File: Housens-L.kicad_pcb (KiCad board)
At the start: 4 copper layers, 50 x 50 mm, 47 parts, among them J1 JTAG/SWD, J2 USB_C_2.0, Q1 BSS138DWQ, SW1 RESET, SW2 USER, U1 MCP1603, U2 BME280, U3 OPT3005, U4 STM32WB55CGUx, U5 STCC4, U6 REG710NA-3.3, Y1 32MHz, Y2 32.768kHz

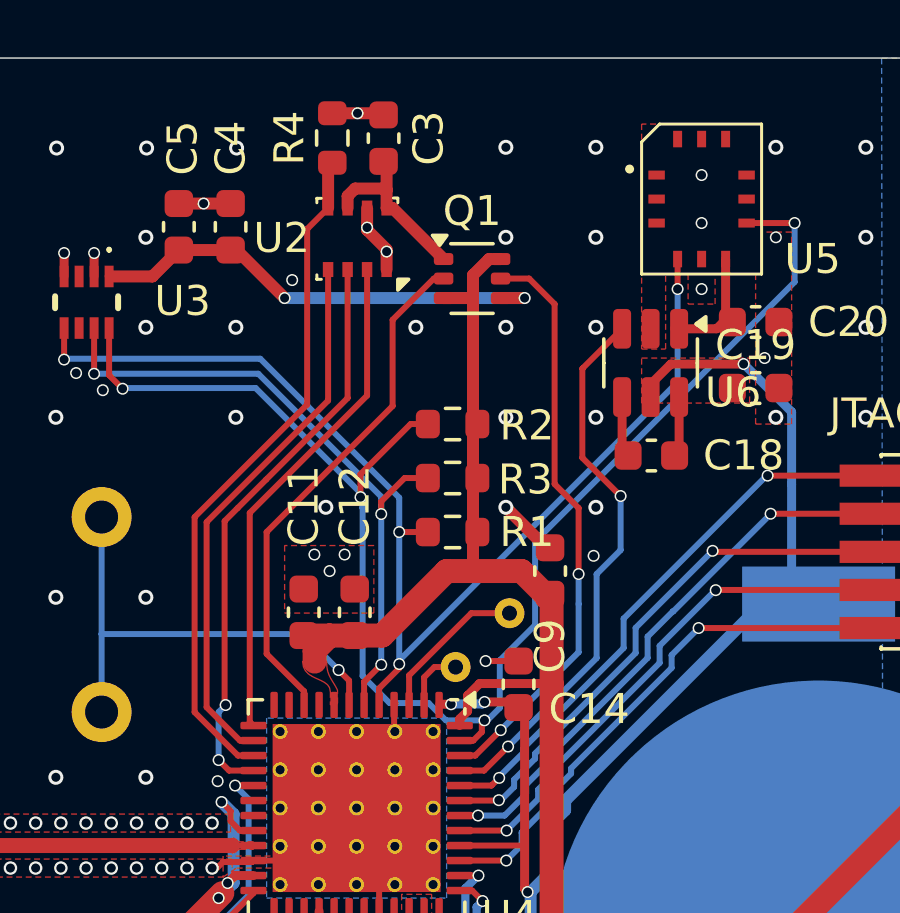
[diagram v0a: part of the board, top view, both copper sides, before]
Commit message: Use proper load switch instead of plain FET
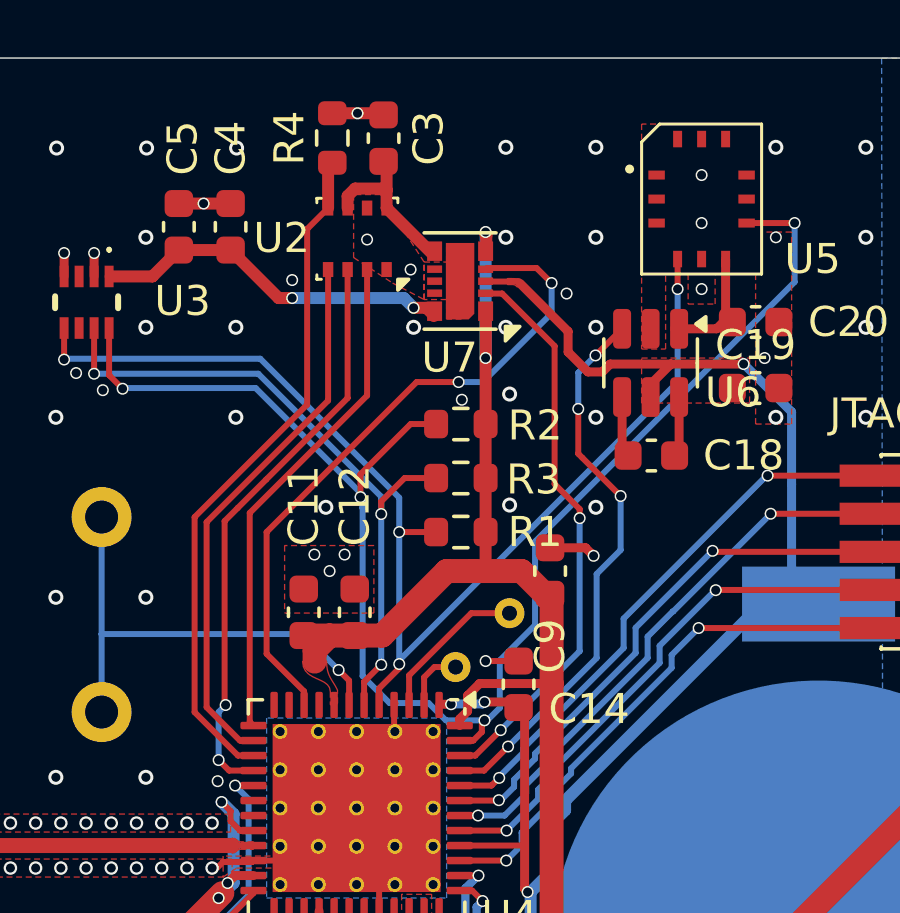
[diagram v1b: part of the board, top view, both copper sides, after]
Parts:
- removed Q1: BSS138DWQ, Package_TO_SOT_SMD:SOT-363_SC-70-6
- added U7: AP22966, Invented:DFN-14-1EP_3x2mm_P0.4mm_EP1.78x1.35mm_AP22966, F.Cu at (88.5, 87.4)
- moved R1 0.27 mm to (88.5, 95.8)
- moved R2 0.27 mm to (88.5, 92.2)
- moved R3 0.27 mm to (88.5, 94.0)
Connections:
- AE1 pad 2: GND -> (no net)
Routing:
- net +BATT: track 55.4 -> 63.2 mm
- net /~{ATMO_EN}: track 17.4 -> 22.2 mm, vias 0 -> 2
- net Net-(U3-VDD): track 15.6 -> 12.1 mm
- net GND: track 44.4 -> 41.6 mm, vias 164 -> 166
- net +1V8: track 109.1 -> 109.7 mm, vias 3 -> 5
- net /~{CO2_EN}: track 18.5 -> 18.6 mm, vias 2 -> 4

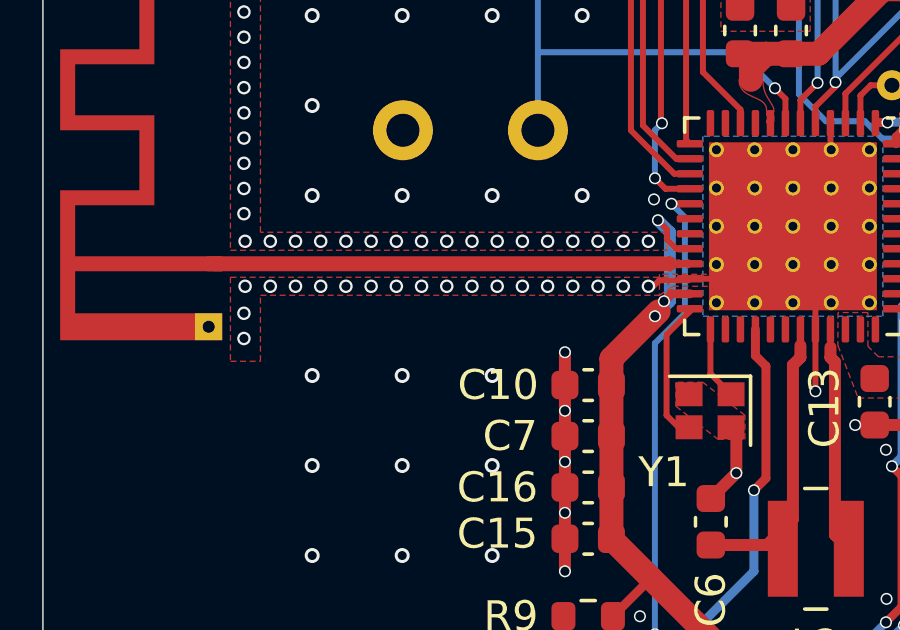
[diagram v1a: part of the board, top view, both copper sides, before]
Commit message: Add matching circuit to antenna
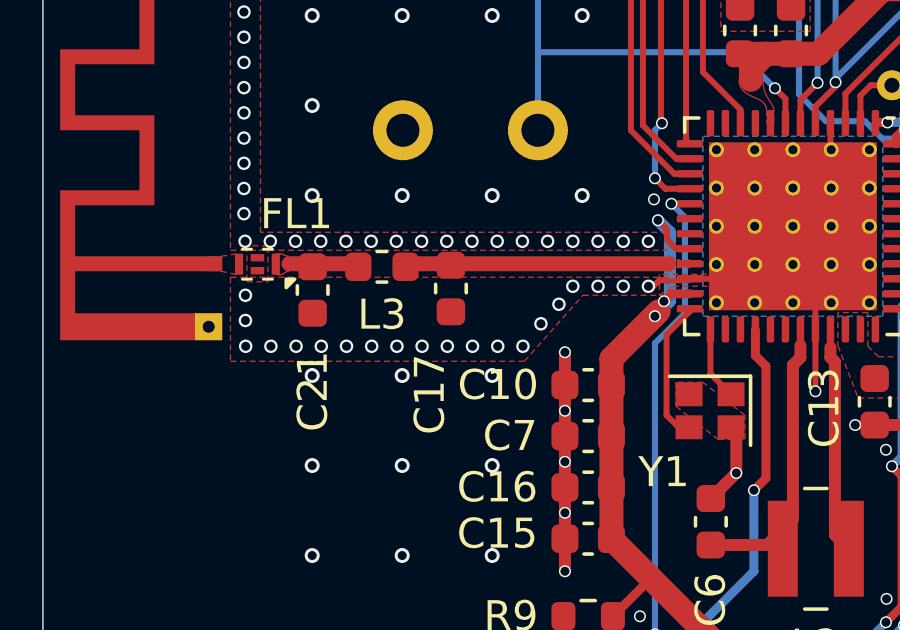
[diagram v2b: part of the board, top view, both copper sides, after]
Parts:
- added C17: 0.8p, Capacitor_SMD:C_0603_1608Metric, F.Cu at (73.6, 107.1)
- added C21: 0.3p, Capacitor_SMD:C_0603_1608Metric, F.Cu at (69.0, 107.1)
- added FL1: DLF162500LT-5028A1, Invented:DLF162500LT-5028A1, F.Cu at (67.2, 106.3)
- added L3: 2.7n, Inductor_SMD:L_0603_1608Metric, F.Cu at (71.3, 106.3)
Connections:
- U4 pad 21: Net-(AE1-A) -> Net-(U4-RF1)
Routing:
- net Net-(AE1-A): track 15.8 -> 0.00 mm
- net Net-(U4-RF1): track 0.00 -> 8.66 mm
- net Net-(FL1-IN): track 0.00 -> 2.35 mm
- net GND: vias 166 -> 167
- added copper zone on F.Cu, net Net-(FL1-IN)
- added copper zone on F.Cu, net Net-(U4-RF1)

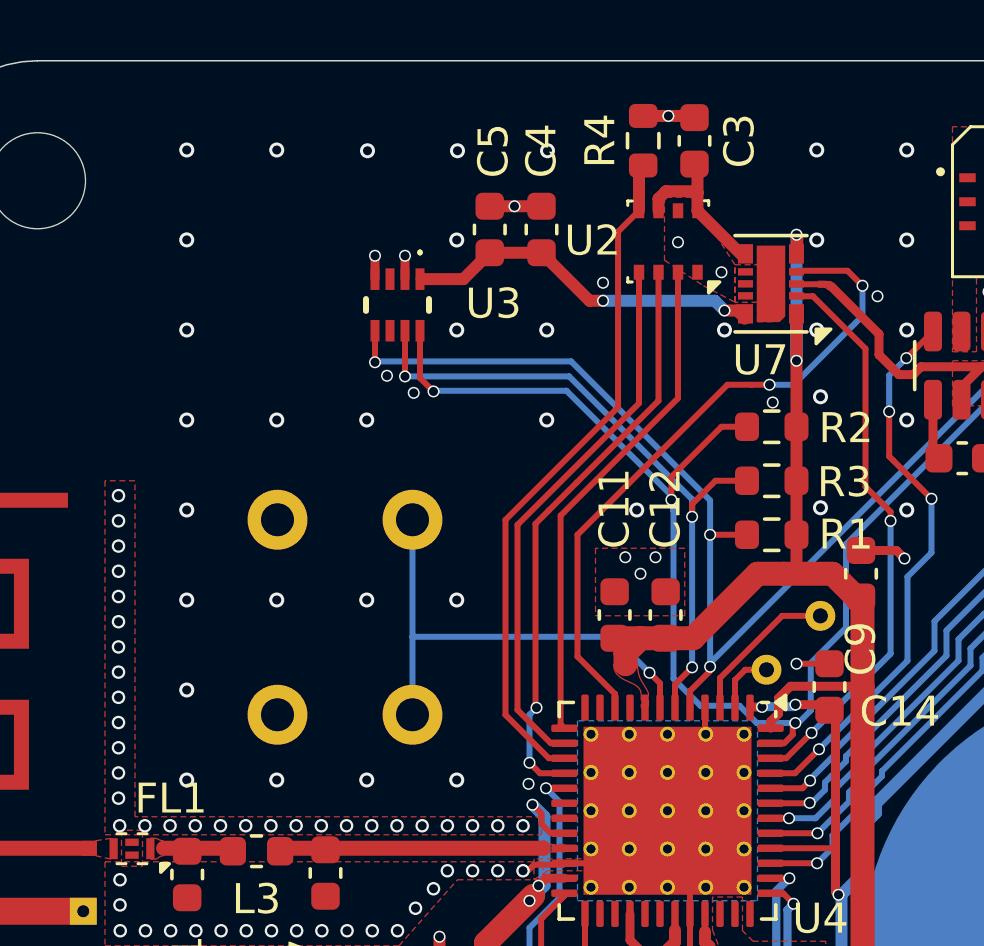
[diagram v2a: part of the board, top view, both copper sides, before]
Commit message: Space out the sensors
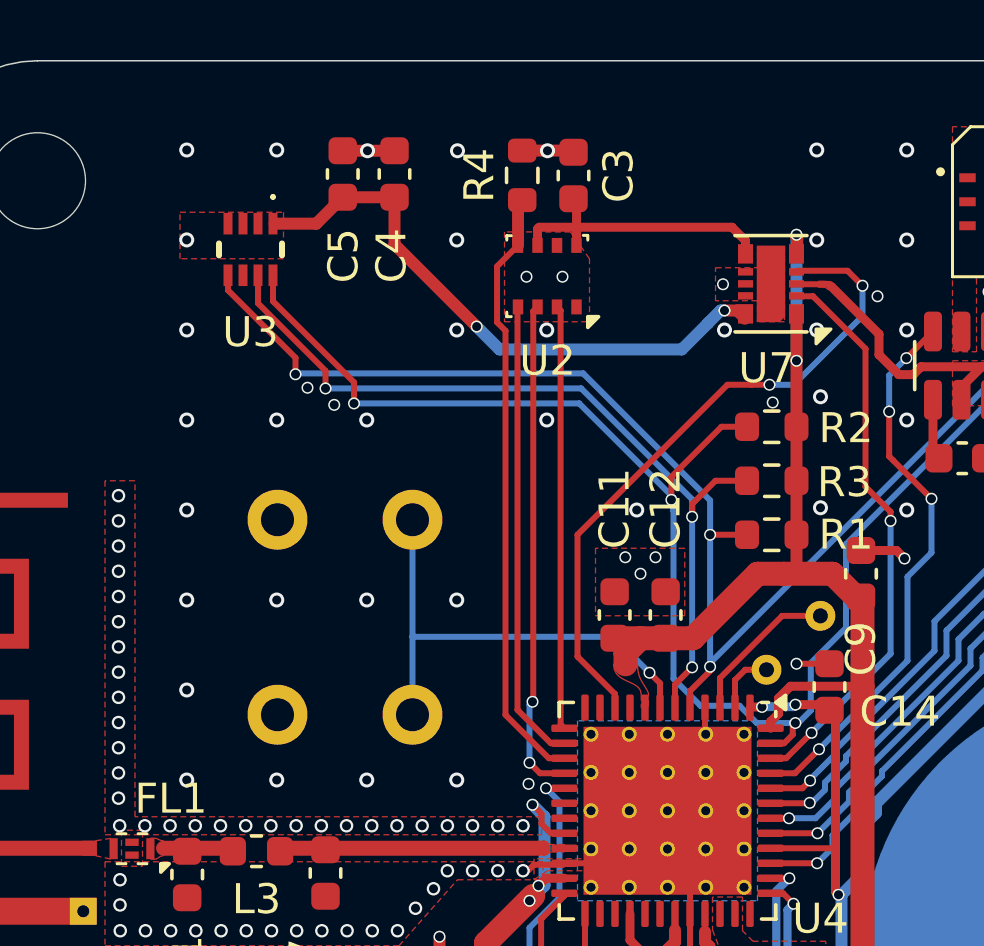
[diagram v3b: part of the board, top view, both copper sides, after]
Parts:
- moved C5 5.24 mm to (74.2, 83.8)
- moved U3 5.24 mm to (71.1, 86.3)
- moved C4 5.24 mm to (75.9, 83.8)
- moved C3 4.19 mm to (81.9, 83.8)
- moved R4 4.19 mm to (80.2, 83.8)
- moved U2 4.19 mm to (81.0, 87.2)
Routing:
- net Net-(U3-VDD): track 12.1 -> 19.7 mm
- net /I2C1_SCL: track 39.6 -> 45.3 mm
- net /OPT_INT: track 22.3 -> 27.9 mm
- net /I2C1_SDA: track 50.3 -> 55.9 mm
- net Net-(U2-VDD): track 5.56 -> 9.56 mm
- net /SPI1_SDO: track 19.5 -> 16.6 mm
- net /SPI1_CLK: track 18.3 -> 15.5 mm
- net /SPI1_CS: track 16.9 -> 14.1 mm
- net /SPI1_SDI: track 22.8 -> 20.2 mm
- net GND: track 41.6 -> 40.0 mm, vias 167 -> 163

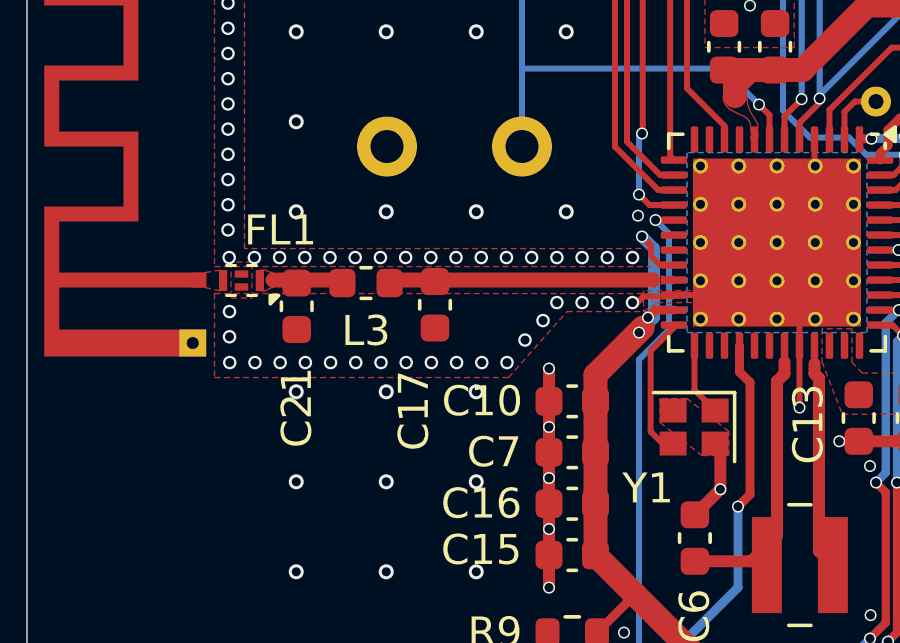
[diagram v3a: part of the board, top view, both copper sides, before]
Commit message: Replace matching circuit with IPD
This is more compact, purpose-made, and cheaper than the individual components!
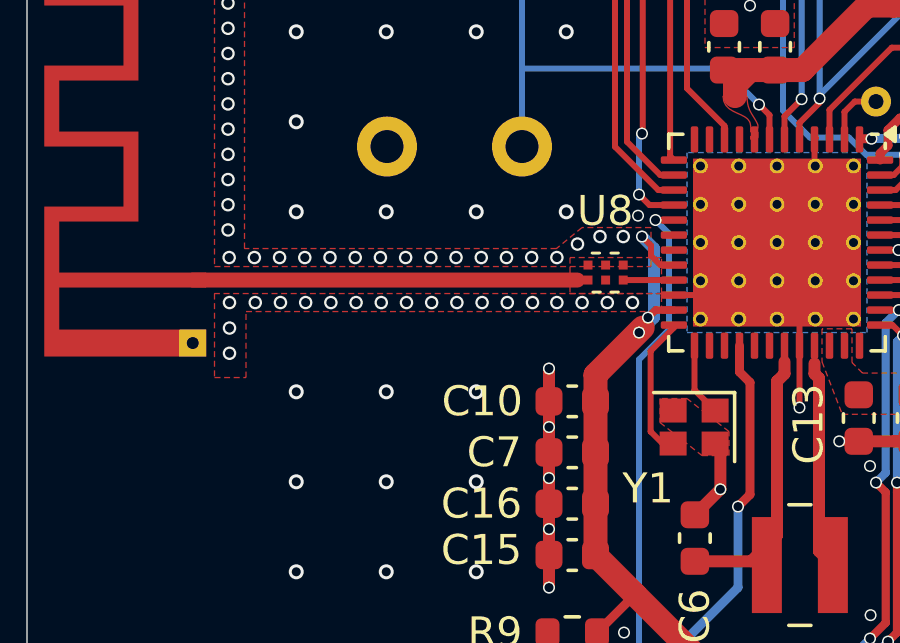
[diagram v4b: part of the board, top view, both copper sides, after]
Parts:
- removed C17: 0.8p, Capacitor_SMD:C_0603_1608Metric
- removed C21: 0.3p, Capacitor_SMD:C_0603_1608Metric
- removed FL1: DLF162500LT-5028A1, Invented:DLF162500LT-5028A1
- removed L3: 2.7n, Inductor_SMD:L_0603_1608Metric
- added U8: MLPF-WB55-01E3, Invented:MLPF-WB55-01E3, F.Cu at (79.3, 106.0)
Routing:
- net Net-(AE1-A): track 0.00 -> 12.3 mm
- net Net-(U4-RF1): track 8.66 -> 1.69 mm
- net Net-(FL1-IN): track 2.35 -> 0.00 mm
- net GND: track 40.0 -> 38.7 mm, vias 163 -> 162
- removed copper zone on F.Cu, net Net-(AE1-A)
- removed copper zone on F.Cu, net Net-(FL1-IN)
- removed copper zone on F.Cu, net Net-(U4-RF1)

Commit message: Use LM voltage reg instead of unobtainium MCP
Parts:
- U1: value MCP1603 -> LM3670MF; footprint Package_TO_SOT_SMD:SOT-23-5 -> Package_TO_SOT_SMD:TSOT-23-5

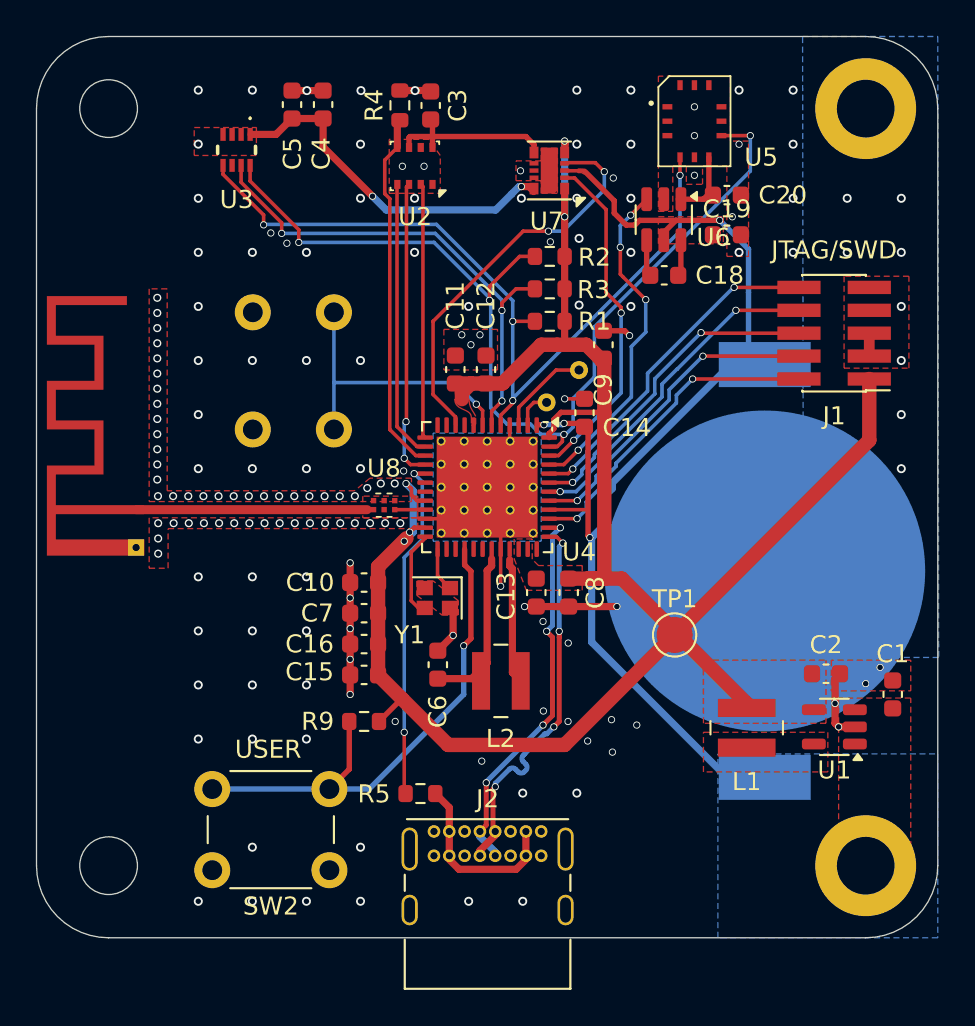
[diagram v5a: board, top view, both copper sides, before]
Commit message: Add RPi-style debug port
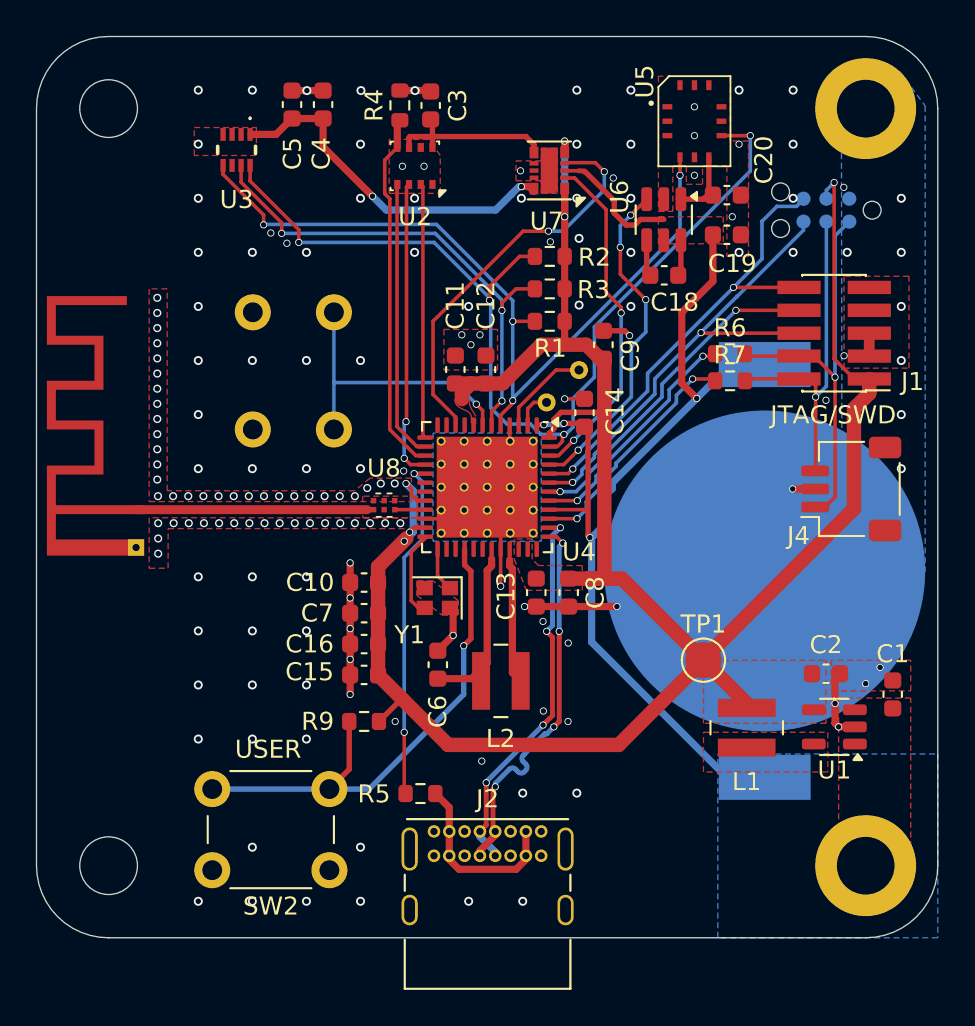
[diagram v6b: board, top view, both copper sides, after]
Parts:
- added J3: RPI_SWD, Connector:Tag-Connect_TC2030-IDC-NL_2x03_P1.27mm_Vertical, B.Cu at (103.8, 89.6)
- added J4: RPI_SWD, Connector_JST:JST_SH_SM03B-SRSS-TB_1x03-1MP_P1.00mm_Horizontal, F.Cu at (105.2, 105.1)
- added R6: 100, Resistor_SMD:R_0603_1608Metric, F.Cu at (98.5, 97.6)
- added R7: 100, Resistor_SMD:R_0603_1608Metric, F.Cu at (98.5, 99.1)
- added REF**: KiCad-Logo2_6mm_SilkScreen, Symbol:KiCad-Logo2_6mm_SilkScreen, B.Cu at (73.8, 111.1)
- added REF**: OSHW-Logo2_7.3x6mm_SilkScreen, Symbol:OSHW-Logo2_7.3x6mm_SilkScreen, B.Cu at (85.0, 118.5)
- moved TP1 2.13 mm to (97.0, 114.6)
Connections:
- J1 pad 2: /SWDIO_JTMS -> Net-(J1-SWDIO/TMS)
- J1 pad 4: /SWCLK_JTCK -> Net-(J1-SWCLK/TCK)
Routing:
- net Net-(J1-SWCLK/TCK): track 0.00 -> 22.4 mm, vias 0 -> 1
- net Net-(J1-SWDIO/TMS): track 0.00 -> 18.8 mm, vias 0 -> 1
- net +1V8: track 109.3 -> 124.3 mm, vias 5 -> 6
- net /SWTRACE_JTDO: track 18.1 -> 26.6 mm
- net /JTRST: track 18.8 -> 26.0 mm
- net /SWDIO_JTMS: track 17.9 -> 13.3 mm
- net /SWCLK_JTCK: track 17.8 -> 13.2 mm
- net +BATT: track 63.2 -> 61.1 mm
- net GND: track 38.7 -> 39.9 mm, vias 162 -> 160
- net (no net): vias 0 -> 1
